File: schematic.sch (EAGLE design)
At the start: 17 parts, among them IC1 AD8015

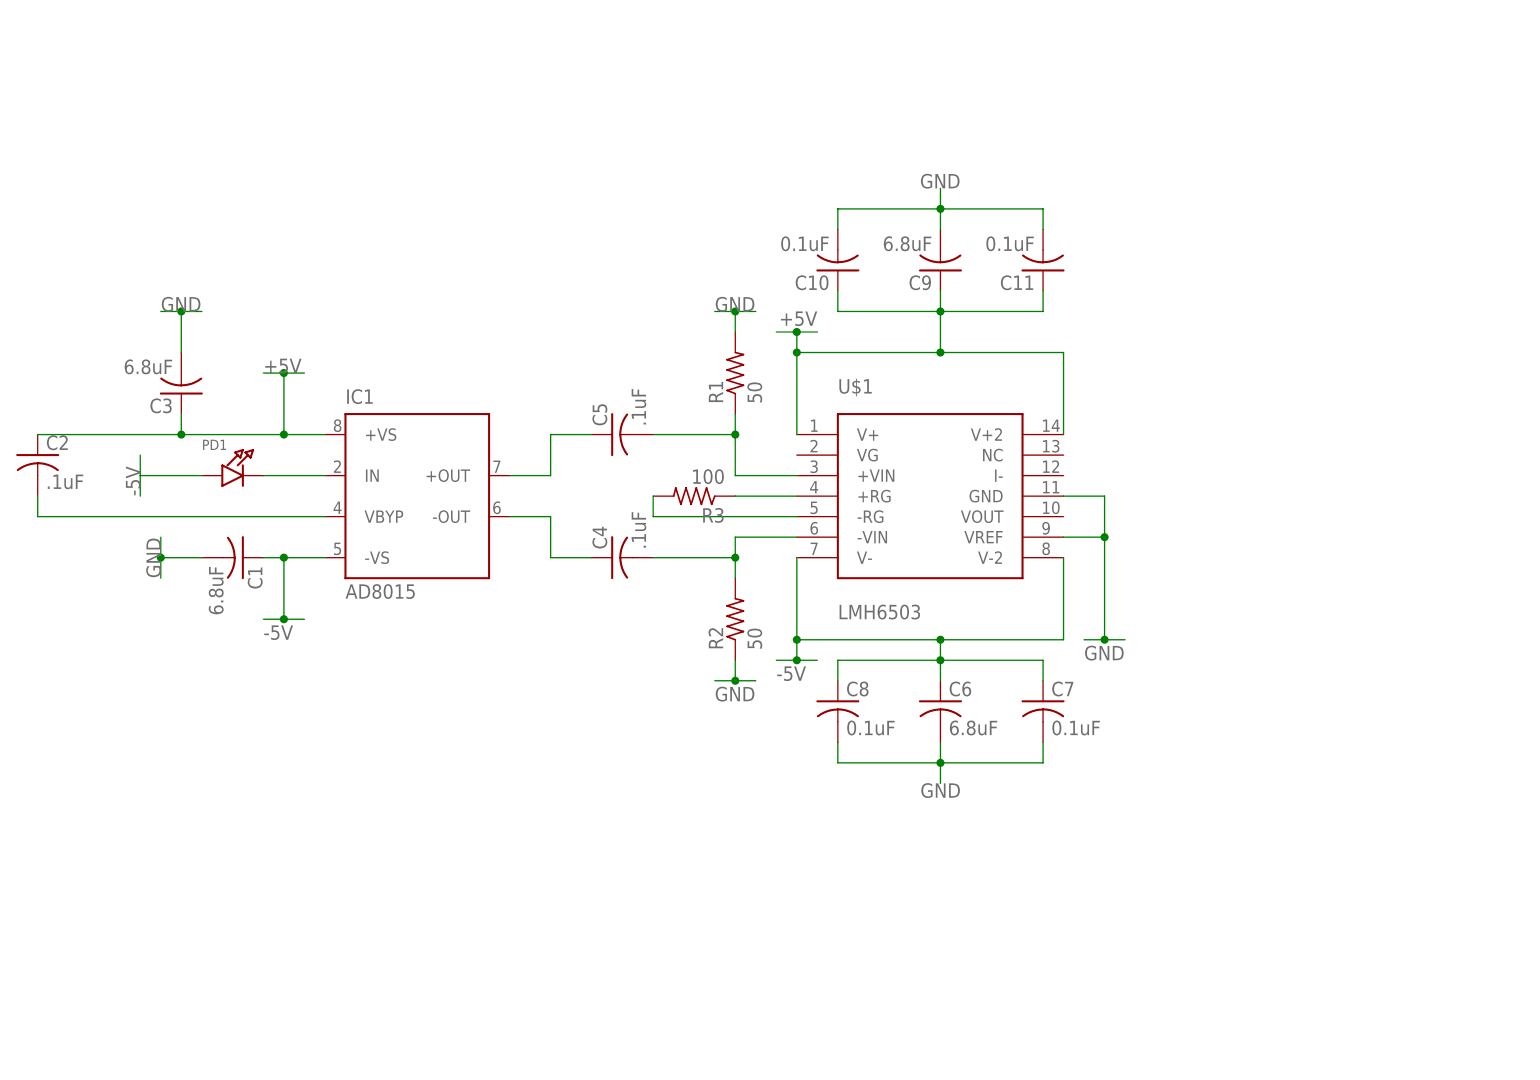
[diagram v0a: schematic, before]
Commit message: Finished main schematic
Still to layout and copy three times
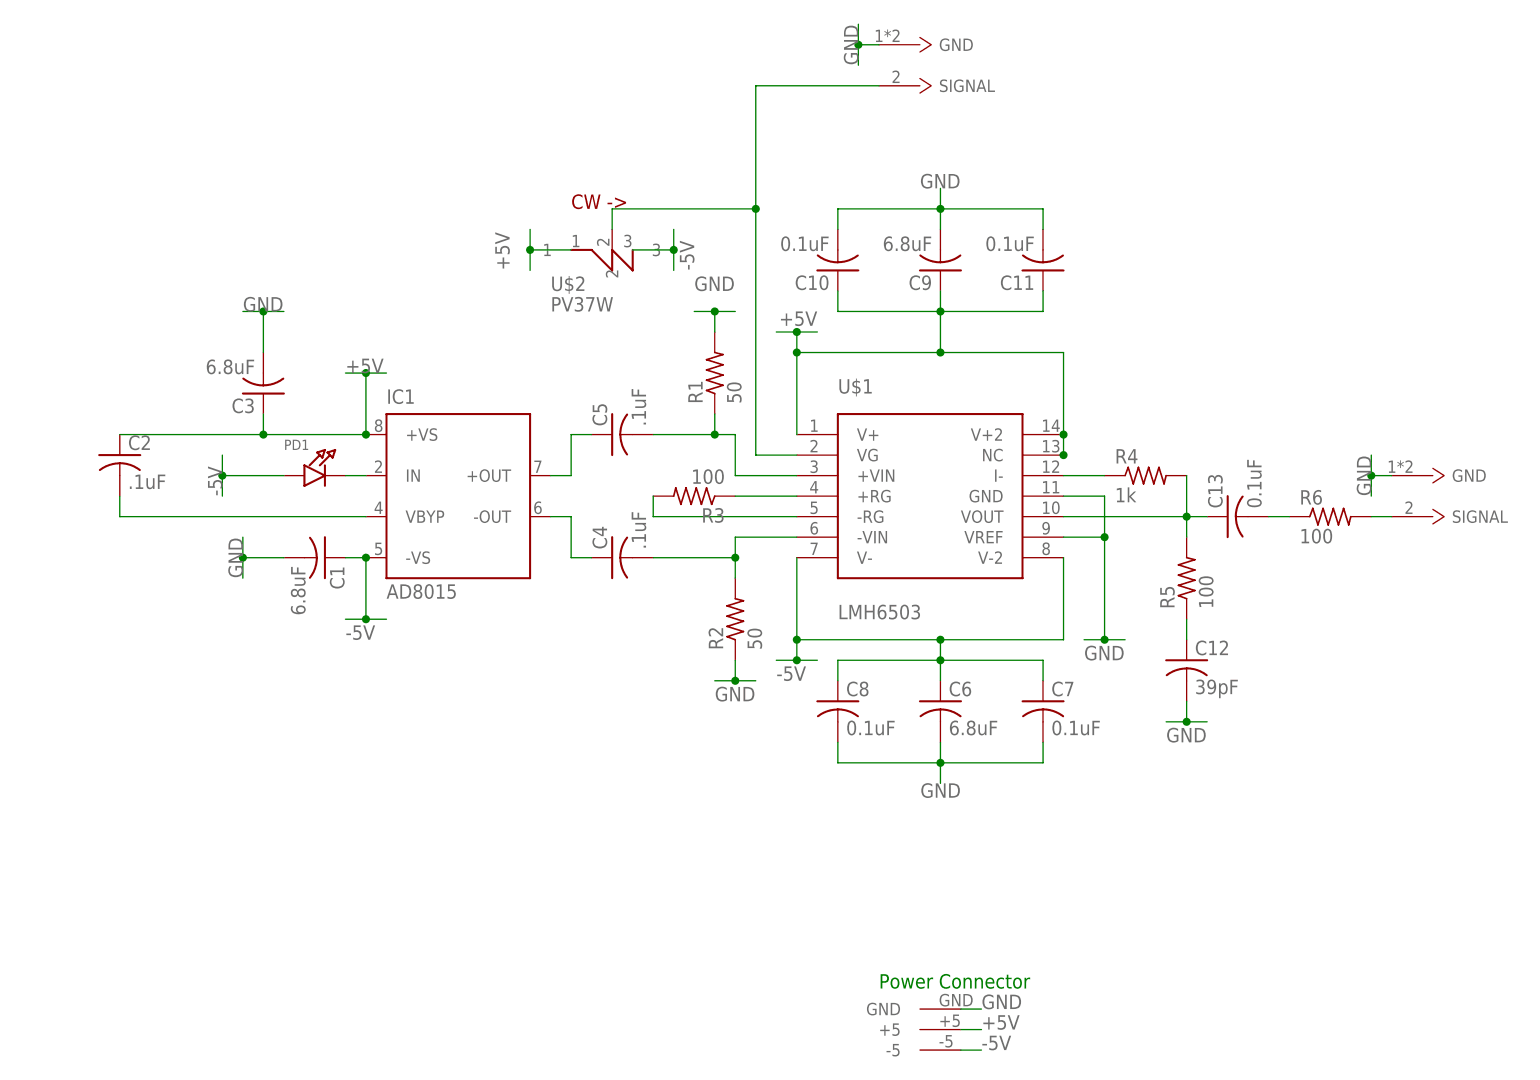
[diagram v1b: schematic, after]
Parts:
- added C12: 39pF, rcl:C-USC0603
- added C13: 0.1uF, rcl:C-USC0603
- added R4: 1k, rcl:R-US_R0603
- added R5, R6: 100, rcl:R-US_R0603
- added U$2: PV37W, 12-ChannelEMG:PV37W
- added U$3: DIVERSITYPWR, 12-ChannelEMG:DIVERSITYPWR
- added U$4, U$5: BNCCONN, 12-ChannelEMG:BNCCONN
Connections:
- new net N$10: C13.1, R4.2, R5.2, U$1.VOUT
- new net N$11: C12.1, R5.1
- new net N$12: C13.2, R6.1
- new net N$13: U$1.VG, U$2.2, U$4.SIGNAL
- new net N$14: R6.2, U$5.SIGNAL
- new net N$9: R4.1, U$1.I-
- net +5V: now also U$1.NC, U$2.1, U$3.+5
- net -5V: now also U$2.3, U$3.-5
- net GND: now also C12.2, U$3.GND, U$4.GND, U$5.GND
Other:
- note added: "Power Connector"
- moved on the sheet: C1, C2, C3, IC1, PD1, R1

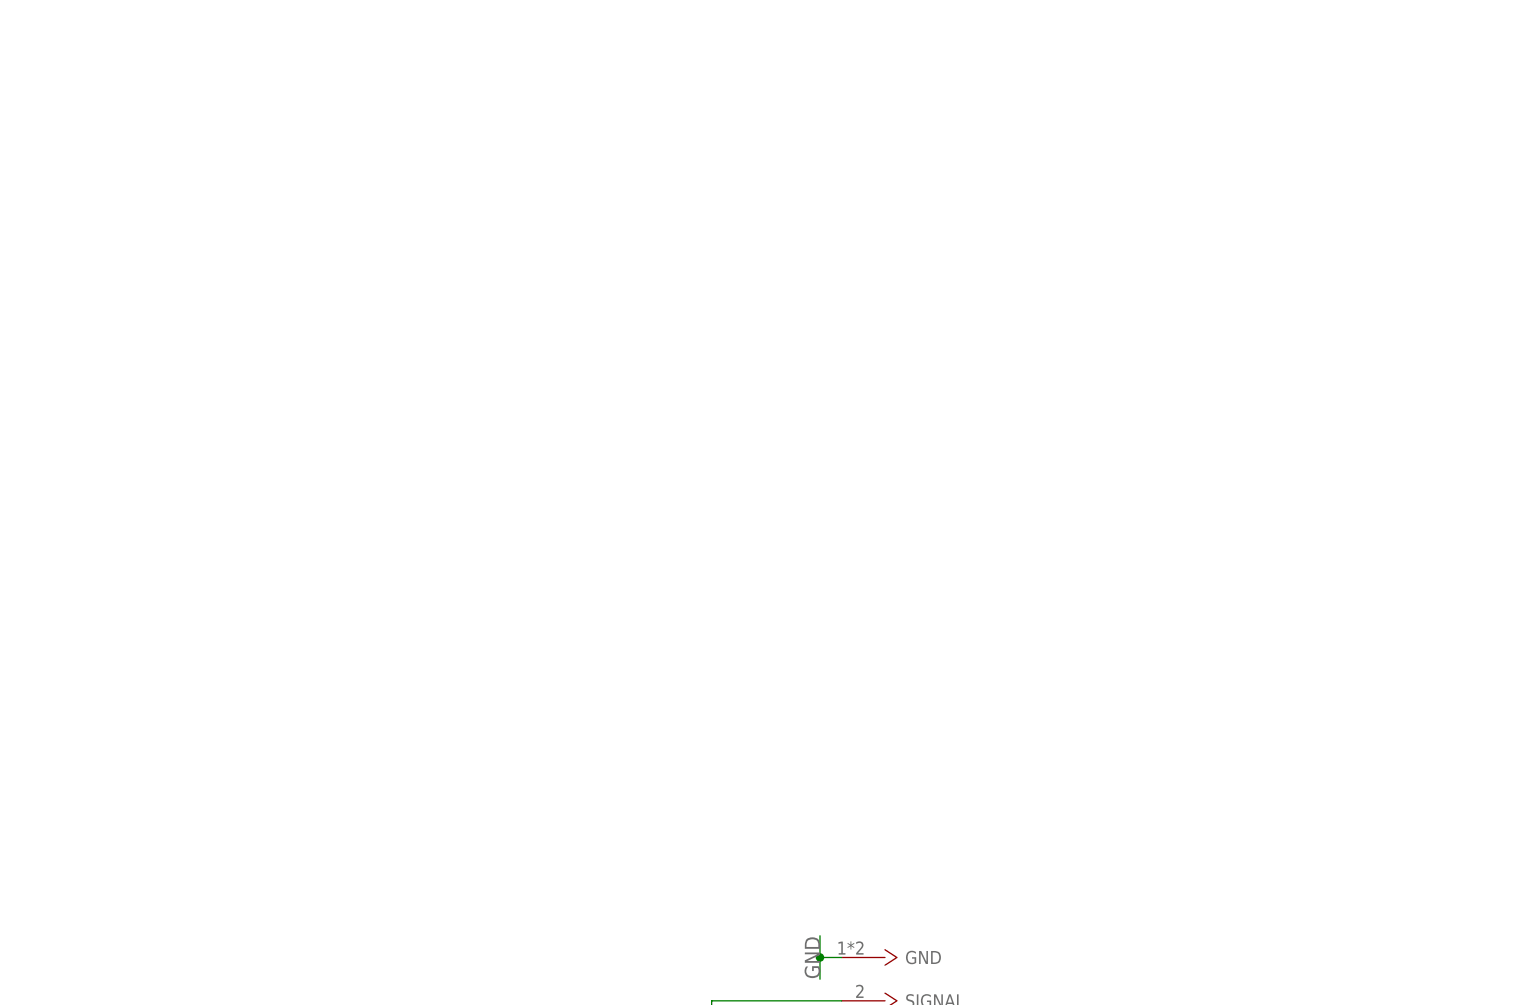
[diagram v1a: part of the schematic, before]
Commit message: Fixed DRC Error and second circuit
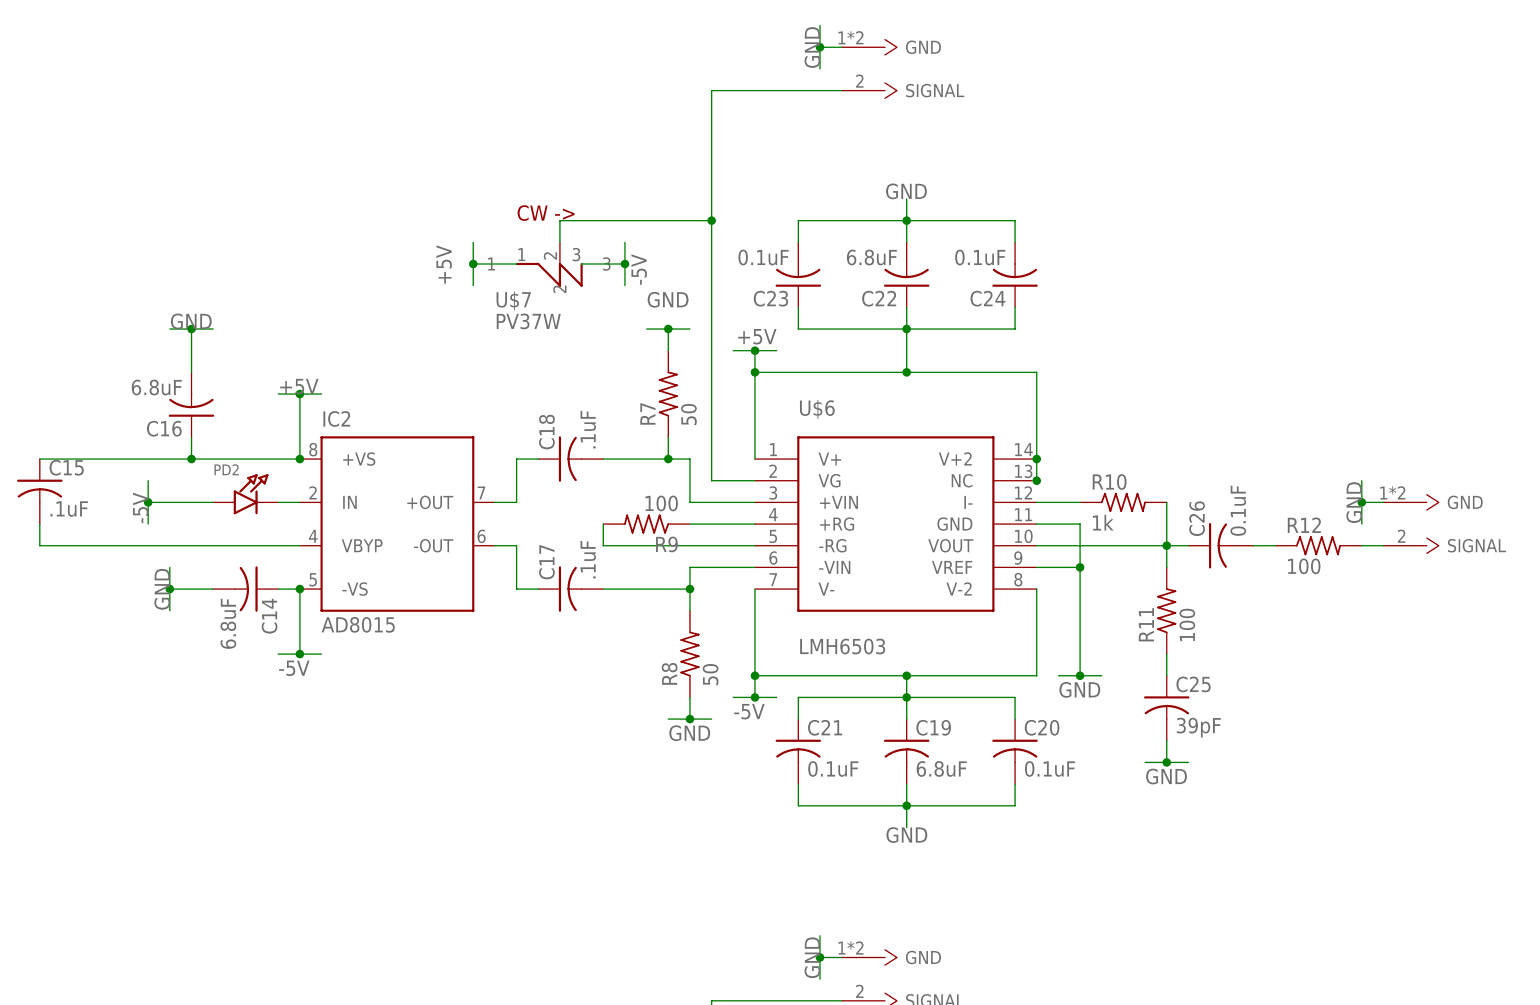
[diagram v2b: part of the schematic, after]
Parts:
- added C14, C16, C19, C22: 6.8uF, rcl:C-USC1206
- added C15, C17, C18: .1uF, rcl:C-USC0603
- added C20, C23: 0.1uF, rcl:C-USC0402
- added C21, C24, C26: 0.1uF, rcl:C-USC0603
- added C25: 39pF, rcl:C-USC0603
- added IC2: AD8015, analog-devices:AD8015
- added PD2: (no value), microbuilder:LED1206
- added R10: 1k, rcl:R-US_R0603
- added R11, R12, R9: 100, rcl:R-US_R0603
- added R7, R8: 50, rcl:R-US_R0603
- added U$6: LMH6503, 12-ChannelEMG:LMH6503
- added U$7: PV37W, 12-ChannelEMG:PV37W
- added U$8, U$9: BNCCONN, 12-ChannelEMG:BNCCONN
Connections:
- new net N$15: C15.2, IC2.VBYP
- new net N$16: IC2.IN, PD2.C
- new net N$17: C18.1, IC2.+OUT
- new net N$18: C17.1, IC2.-OUT
- new net N$19: C17.2, R8.2, U$6.-VIN
- new net N$20: C18.2, R7.1, U$6.+VIN
- new net N$21: R9.1, U$6.+RG
- new net N$22: R9.2, U$6.-RG
- new net N$23: R10.1, U$6.I-
- new net N$24: C26.1, R10.2, R11.2, U$6.VOUT
- new net N$25: C25.1, R11.1
- new net N$26: C26.2, R12.1
- new net N$27: U$6.VG, U$7.2, U$8.SIGNAL
- new net N$28: R12.2, U$9.SIGNAL
- net +5V: now also C15.1, C16.1, C22.1, C23.1, C24.1, IC2.+VS, U$6.NC, U$6.V+, U$6.V+2, U$7.1
- net -5V: now also C14.1, C19.1, C20.1, C21.1, IC2.-VS, PD2.A, U$6.V-, U$6.V-2, U$7.3
- net GND: now also C14.2, C16.2, C19.2, C20.2, C21.2, C22.2, C23.2, C24.2, C25.2, R7.2, R8.1, U$6.GND, U$6.VREF, U$8.GND, U$9.GND
